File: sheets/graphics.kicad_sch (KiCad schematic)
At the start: 25 parts, among them J2 CUT DOG, SW1 RESET SWITCH, U13 NEO-B1, U14 PST518B, U15 74LS244, U16 TC531000AP, U17 uPD43256AGU-12L, U18 uPD43256AGU-12L, U19 CXK5864P-35, U20 CXK5864P-35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

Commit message: Update BF1.4
Update Mouser Parts
Update Silkscreen for Memory Slot
Update Silkscreen for BF1.4 Version and date
Generate Gerbers and BOM files
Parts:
- R28: Mouser (none) -> 594-5063JD10K1%TR
- R29: Mouser (none) -> 594-5063JD47R00F
- R5814: Comment Fitted if -> Fitted if either 5814 or 5863 link for RAM type
- R5863: Comment (none) -> Fitted if either 5814 or 5863 link for RAM type
- U17, U18: Alternative (none) -> JEDEC 62256 (32k x 8) SRAM; Mouser (none) -> 870-62C256AL-25ULI
- U19, U20: Alternative (none) -> JEDEC 6116 (2k x 8) SRAM 35ns
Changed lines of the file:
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@@
   (title_block
     (title "NeoGeo AES 3-5")
-    (date "2023-12-30")
-    (rev "BF1.3")
+    (date "2024-01-06")
+    (rev "BF1.4")
     (company "SNK")
     (comment 3 "https://github.com/Board-Folk")
@@
       (effects (font (size 1.27 1.27)) hide)
     )
-    (property "Mouser" "" (at 60.198 77.216 0)
+    (property "Mouser" "870-62C256AL-25ULI" (at 60.198 77.216 0)
       (effects (font (size 1.27 1.27)) hide)
     )
-    (property "Alternative" "" (at 60.198 77.216 0)
+    (property "Alternative" "JEDEC 62256 (32k x 8) SRAM" (at 60.198 77.216 0)
       (effects (font (size 1.27 1.27)) hide)
     )
@@
       (effects (font (size 1.27 1.27)) hide)
     )
-    (property "Mouser" "" (at 325.628 61.976 0)
+    (property "Mouser" "594-5063JD10K1%TR" (at 325.628 61.976 0)
       (effects (font (size 1.27 1.27)) hide)
     )
@@
       (effects (font (size 1.27 1.27)) hide)
     )
-    (property "Alternative" "" (at 45.212 242.316 0)
+    (property "Alternative" "JEDEC 6116 (2k x 8) SRAM 35ns" (at 45.212 242.316 0)
       (effects (font (size 1.27 1.27)) hide)
     )
@@
       (effects (font (size 1.27 1.27)) hide)
     )
-    (property "Alternative" "" (at 45.212 188.976 0)
+    (property "Alternative" "JEDEC 6116 (2k x 8) SRAM 35ns" (at 45.212 188.976 0)
       (effects (font (size 1.27 1.27)) hide)
     )
@@
       (effects (font (size 1.27 1.27)) hide)
     )
+    (property "Comment" "Fitted if either 5814 or 5863 link for RAM type" (at 86.614 221.488 0)
+      (effects (font (size 1.27 1.27)) hide)
+    )
     (pin "1")
     (pin "2")
@@
       (effects (font (size 1.27 1.27)) hide)
     )
-    (property "Comment" "Fitted if " (at 86.614 208.534 0)
+    (property "Comment" "Fitted if either 5814 or 5863 link for RAM type" (at 86.614 208.534 0)
       (effects (font (size 1.27 1.27)) hide)
     )
@@
       (effects (font (size 1.27 1.27)) hide)
     )
-    (property "Mouser" "" (at 60.198 133.096 0)
+    (property "Mouser" "870-62C256AL-25ULI" (at 60.198 133.096 0)
       (effects (font (size 1.27 1.27)) hide)
     )
-    (property "Alternative" "" (at 60.198 133.096 0)
+    (property "Alternative" "JEDEC 62256 (32k x 8) SRAM" (at 60.198 133.096 0)
       (effects (font (size 1.27 1.27)) hide)
     )
@@
       (effects (font (size 1.27 1.27)) hide)
     )
-    (property "Mouser" "" (at 318.516 97.282 0)
+    (property "Mouser" "594-5063JD47R00F" (at 318.516 97.282 0)
       (effects (font (size 1.27 1.27)) hide)
     )

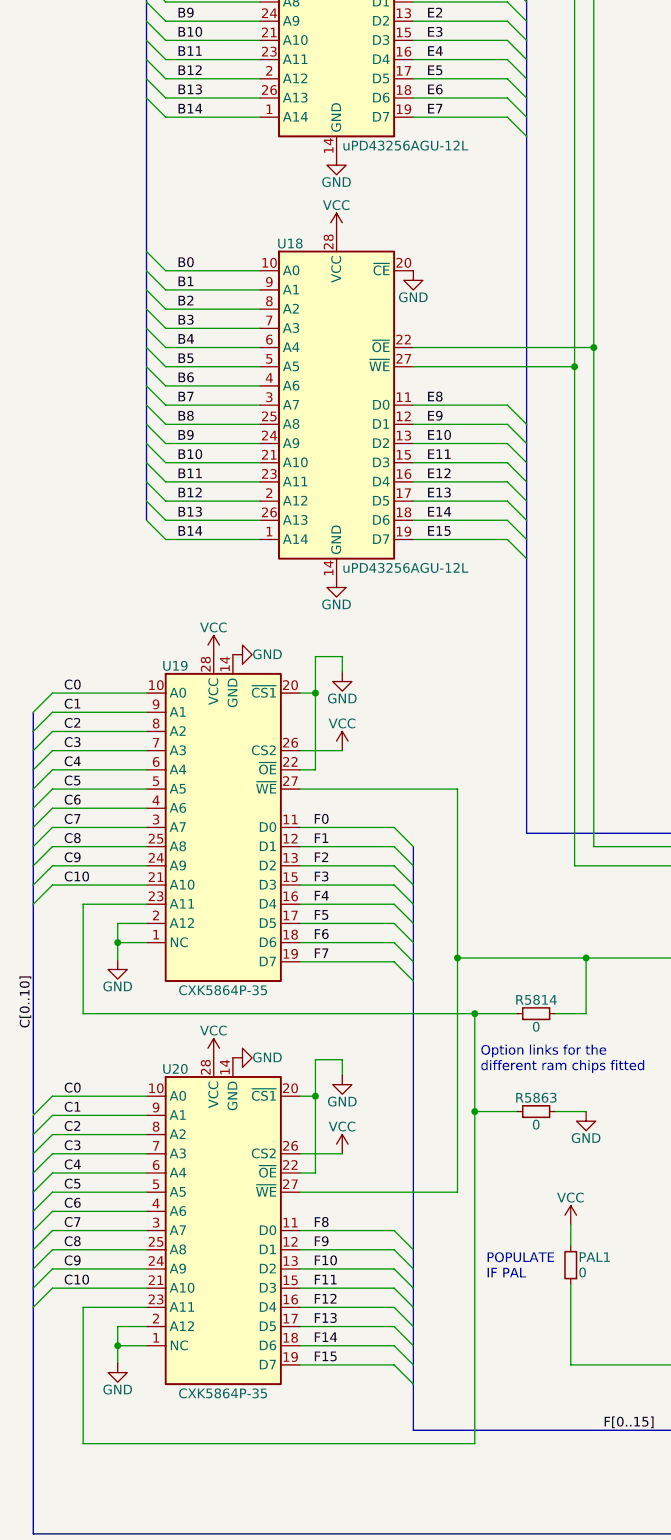
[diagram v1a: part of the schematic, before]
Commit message: Update Silk
Update Ram Silk
Fix mouser wrong 6.8K
Update BOM, Gerbers ...
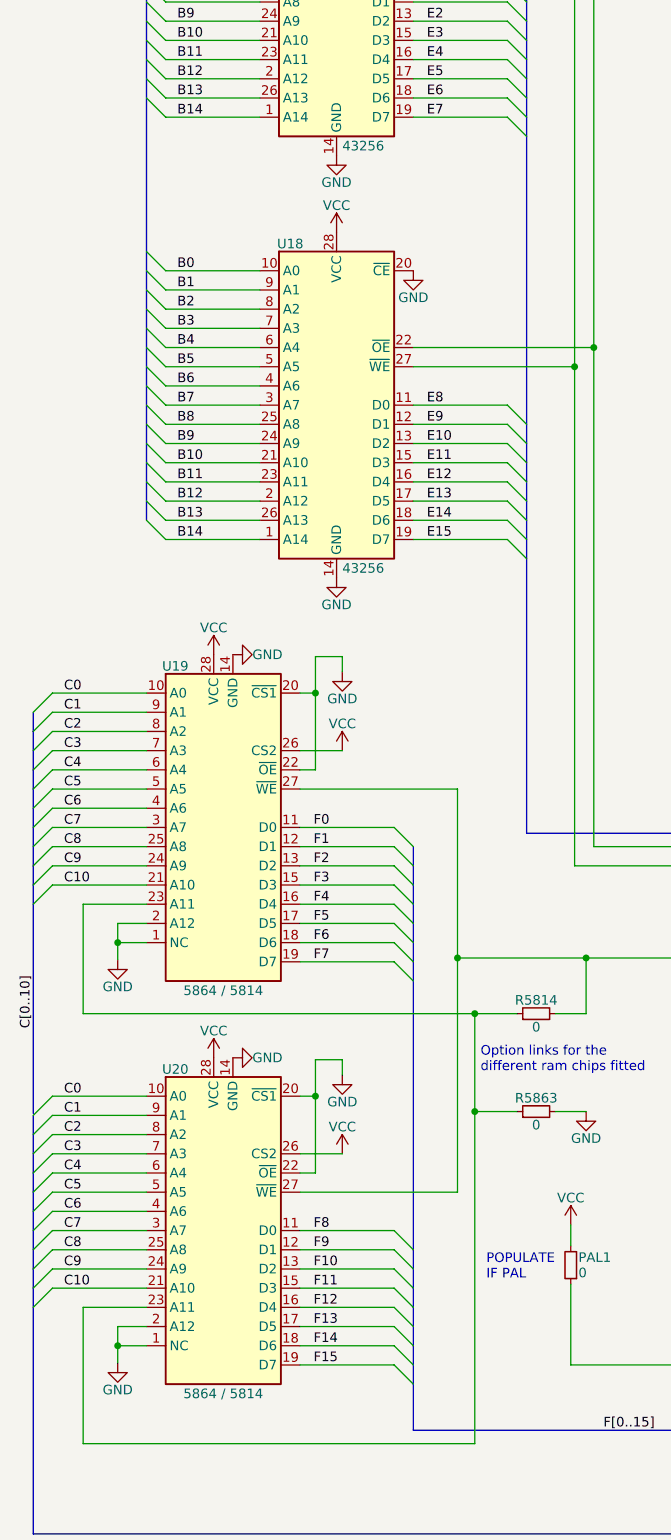
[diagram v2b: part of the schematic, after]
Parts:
- U17, U18: value uPD43256AGU-12L -> 43256
- U19, U20: value CXK5864P-35 -> 5864 / 5814
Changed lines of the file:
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@@
       (effects (font (size 1.27 1.27)) (justify left))
     )
-    (property "Value" "uPD43256AGU-12L" (at 60.96 93.726 0)
+    (property "Value" "43256" (at 60.96 93.726 0)
       (effects (font (size 1.27 1.27)) (justify left))
     )
@@
       (effects (font (size 1.27 1.27)))
     )
-    (property "Value" "CXK5864P-35" (at 45.212 258.826 0)
+    (property "Value" "5864 / 5814" (at 45.212 258.826 0)
       (effects (font (size 1.27 1.27)))
     )
@@
       (effects (font (size 1.27 1.27)))
     )
-    (property "Value" "CXK5864P-35" (at 45.212 205.486 0)
+    (property "Value" "5864 / 5814" (at 45.212 205.486 0)
       (effects (font (size 1.27 1.27)))
     )
@@
       (effects (font (size 1.27 1.27)) (justify left))
     )
-    (property "Value" "uPD43256AGU-12L" (at 60.96 149.606 0)
-      (effects (font (size 1.27 1.27)) (justify left))
-    )
+    (property "Value" "43256" (at 60.96 149.606 0)
+      (effects (font (size 1.27 1.27)) (justify left))
+    )

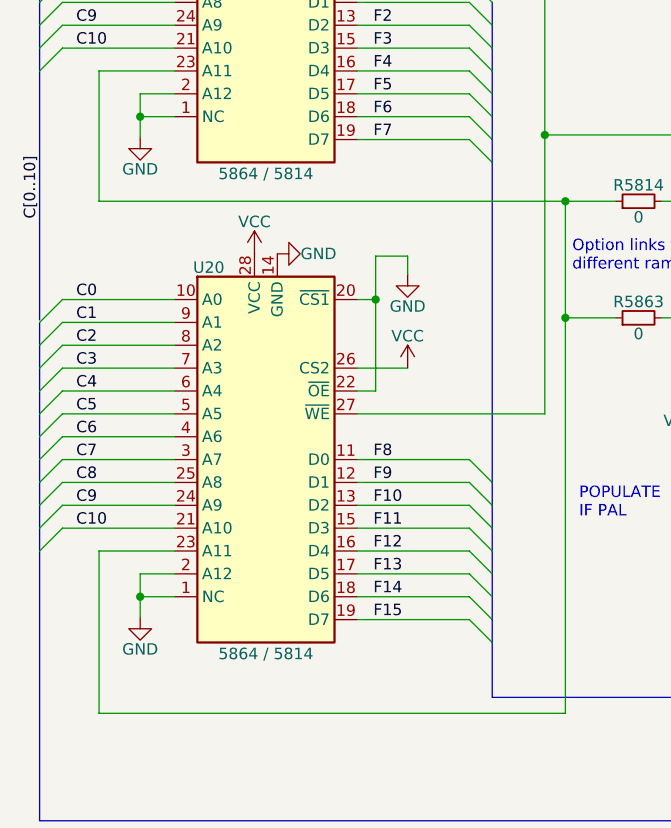
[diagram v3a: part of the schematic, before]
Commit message: Silkscreen change
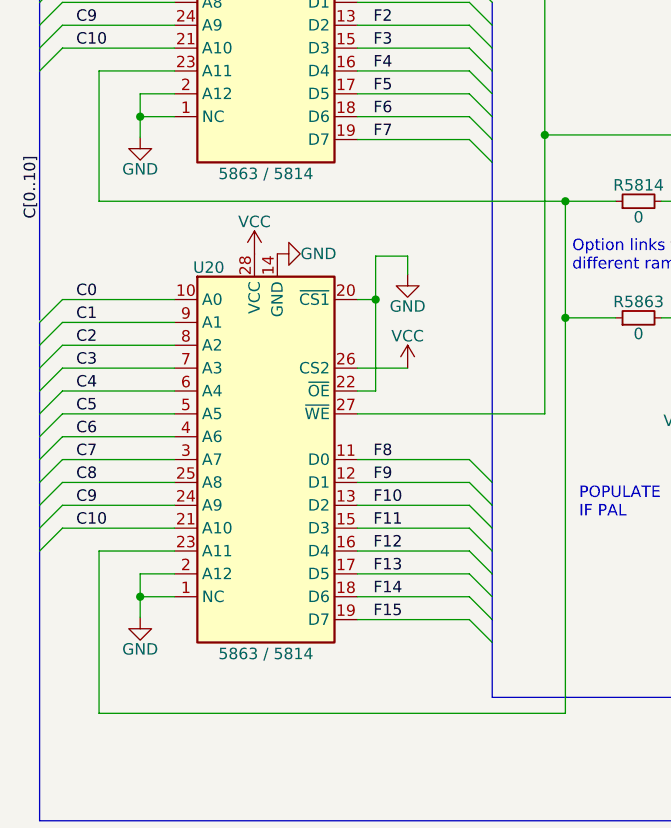
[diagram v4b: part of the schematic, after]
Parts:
- U19, U20: value 5864 / 5814 -> 5863 / 5814
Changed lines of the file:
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@@
       (effects (font (size 1.27 1.27)))
     )
-    (property "Value" "5864 / 5814" (at 45.212 258.826 0)
+    (property "Value" "5863 / 5814" (at 45.212 258.826 0)
       (effects (font (size 1.27 1.27)))
     )
@@
       (effects (font (size 1.27 1.27)))
     )
-    (property "Value" "5864 / 5814" (at 45.212 205.486 0)
-      (effects (font (size 1.27 1.27)))
-    )
+    (property "Value" "5863 / 5814" (at 45.212 205.486 0)
+      (effects (font (size 1.27 1.27)))
+    )
